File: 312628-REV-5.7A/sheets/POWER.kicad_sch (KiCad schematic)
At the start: 79 parts, among them CN504 Jumper_2_Open, CN505 SILPOWER, CN506 POWER, SW501 SW_Push, U1 74LS04, U2 74LS08, U206 7406, U3 74LS14, U325 74LS04, U326 74LS08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

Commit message: update schematics to kicad 7.0.8
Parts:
- renumbered U5 to U207

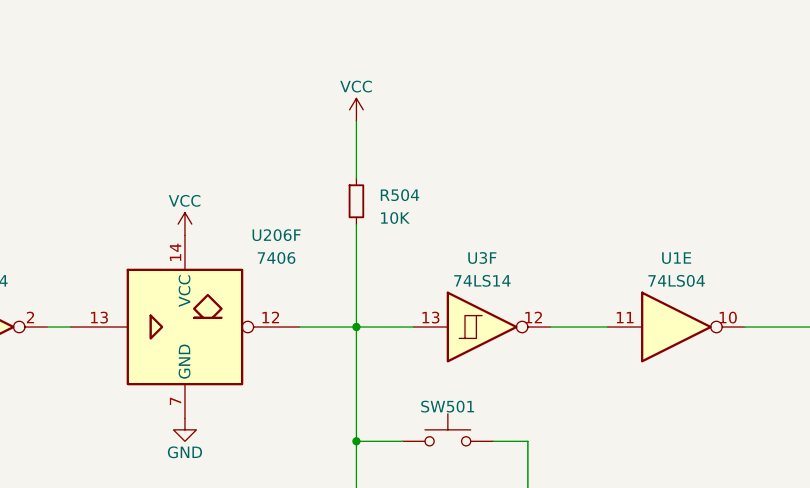
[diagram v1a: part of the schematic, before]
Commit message: Update to latest KiCad 8.0.7
Update to latest KiCad 8.0.7
Fix wrong value of R504 should be 1K
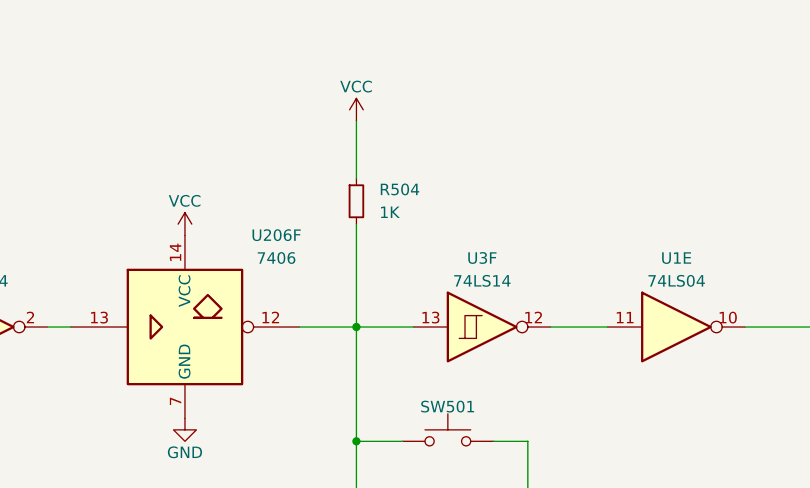
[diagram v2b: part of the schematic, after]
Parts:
- R504: value 10K -> 1K
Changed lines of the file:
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@@
 		(fields_autoplaced yes)
 		(property "Reference" "R504"
-			(at 212.09 34.925 0)
+			(at 212.09 34.2899 0)
 			(effects
 				(font
@@
 			)
 		)
-		(property "Value" "10K"
-			(at 212.09 37.465 0)
+		(property "Value" "1K"
+			(at 212.09 36.8299 0)
 			(effects
 				(font
